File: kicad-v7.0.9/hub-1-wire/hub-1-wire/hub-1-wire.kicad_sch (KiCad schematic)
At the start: 20 parts, among them J1 RJ45, J2 Screw_Terminal_01x03, J3 Screw_Terminal_01x03, J4 Screw_Terminal_01x03, J5 Screw_Terminal_01x03, J6 Screw_Terminal_01x03, J7 Screw_Terminal_01x03, Q1 YJL3415A

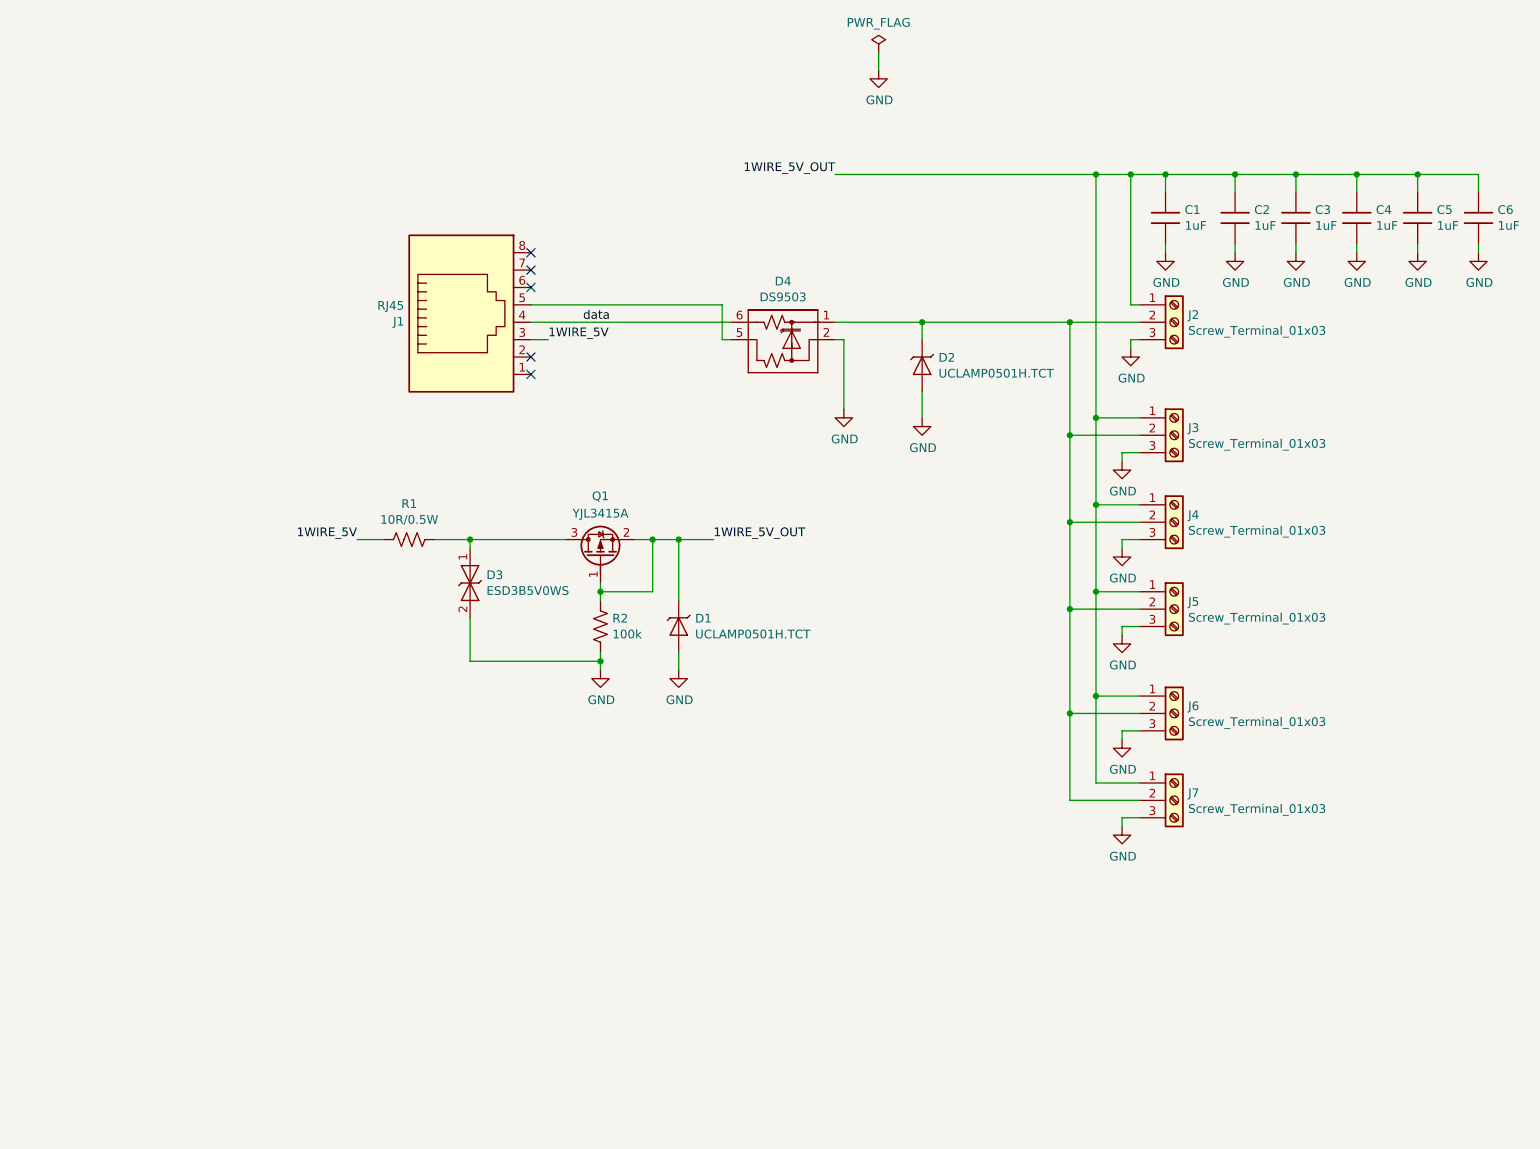
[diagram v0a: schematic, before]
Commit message: 1-Wire bus hub. Change library. Small changes in schematic a PCB.
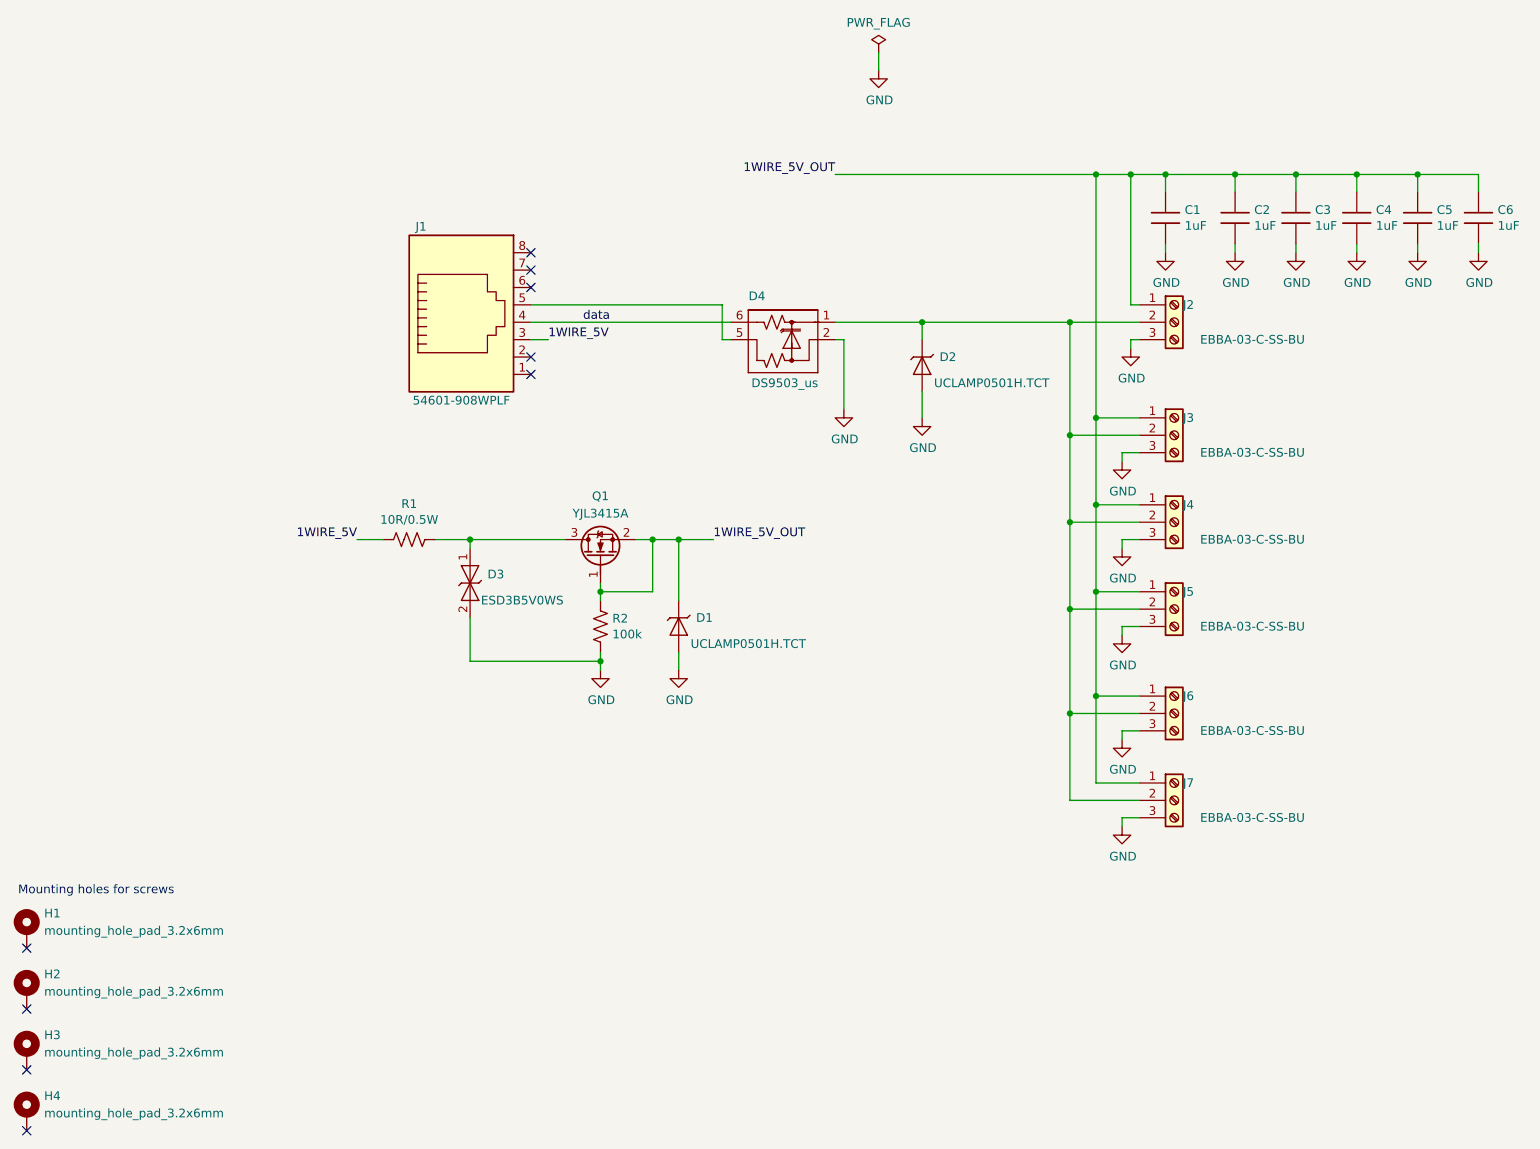
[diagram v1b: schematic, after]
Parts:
- added H1, H2, H3, H4: mounting_hole_pad_3.2x6mm, mounting_hole_pad_rl:mounting_hole_pad_3.2x6mm, symbol mounting_hole_pad_rl:mounting_hole_pad_3.2x6mm
- C1, C2, C3, C4, C5, C6: symbol passive_component_rl:capacitor -> capacitor_smd_rl:c_1206
- D1, D2: symbol diode_rl:undir_transil -> transil_diode_smd_rl:UCLAMP0501H.TCT
- D3: symbol diode_rl:bidir_transil -> transil_diode_smd_rl:ESD3B5V0WS
- D4: value DS9503 -> DS9503_us; symbol diode_rl:DS9503_us -> transil_diode_smd_rl:DS9503_us
- J1: value RJ45 -> 54601-908WPLF; symbol connector_rl:rj45 -> connector_rj45_tht_rl:54601-908WPLF
- J2, J3, J4, J5, J6, J7: value Screw_Terminal_01x03 -> EBBA-03-C-SS-BU; symbol connector_rl:1x3_screw_term_block -> terminal_block_tht_rl:EBBA-03-C-SS-BU
- Q1: symbol unipolar_transistor_rl:p_mosfet_gsd -> unipolar_transistor_smd_rl:YJL3415A
- R1, R2: symbol passive_component_rl:resistor_us -> resistor_smd_rl:r_1206_us
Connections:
- no-connect marks 5 -> 9
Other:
- note added: "Mounting holes for screws"

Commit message: Change of components from edited library.
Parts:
- J1: footprint connector_rl:rj45_54601-908WPLF -> connector_rj45_tht_rl:54601-908WPLF
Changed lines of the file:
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@@
       (effects (font (size 1.27 1.27)))
     )
-    (property "Footprint" "connector_rl:rj45_54601-908WPLF" (at 85.09 50.8 0)
+    (property "Footprint" "connector_rj45_tht_rl:54601-908WPLF" (at 85.09 50.8 0)
       (effects (font (size 1.27 1.27)) hide)
     )
